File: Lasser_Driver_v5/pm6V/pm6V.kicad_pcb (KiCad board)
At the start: 2 copper layers, 160 x 100 mm, 62 parts, among them J4 Screw_Terminal_01x03, J6 DIN41612_M_3x8+8_Power_Male, Q10 Q_NPN MJL21194, Q3 IRF540NPBF, Q4 IRF9540NPBF, Q5 MMBT2907, Q6 MMBT2222, Q7 Q_PNP_MJL21193, Q8 Q_PNP_MJL21193, Q9 Q_NPN MJL21194, U11 LM4051AIM3-ADJ/NOPB, U12 LM4051AIM3-ADJ/NOPB

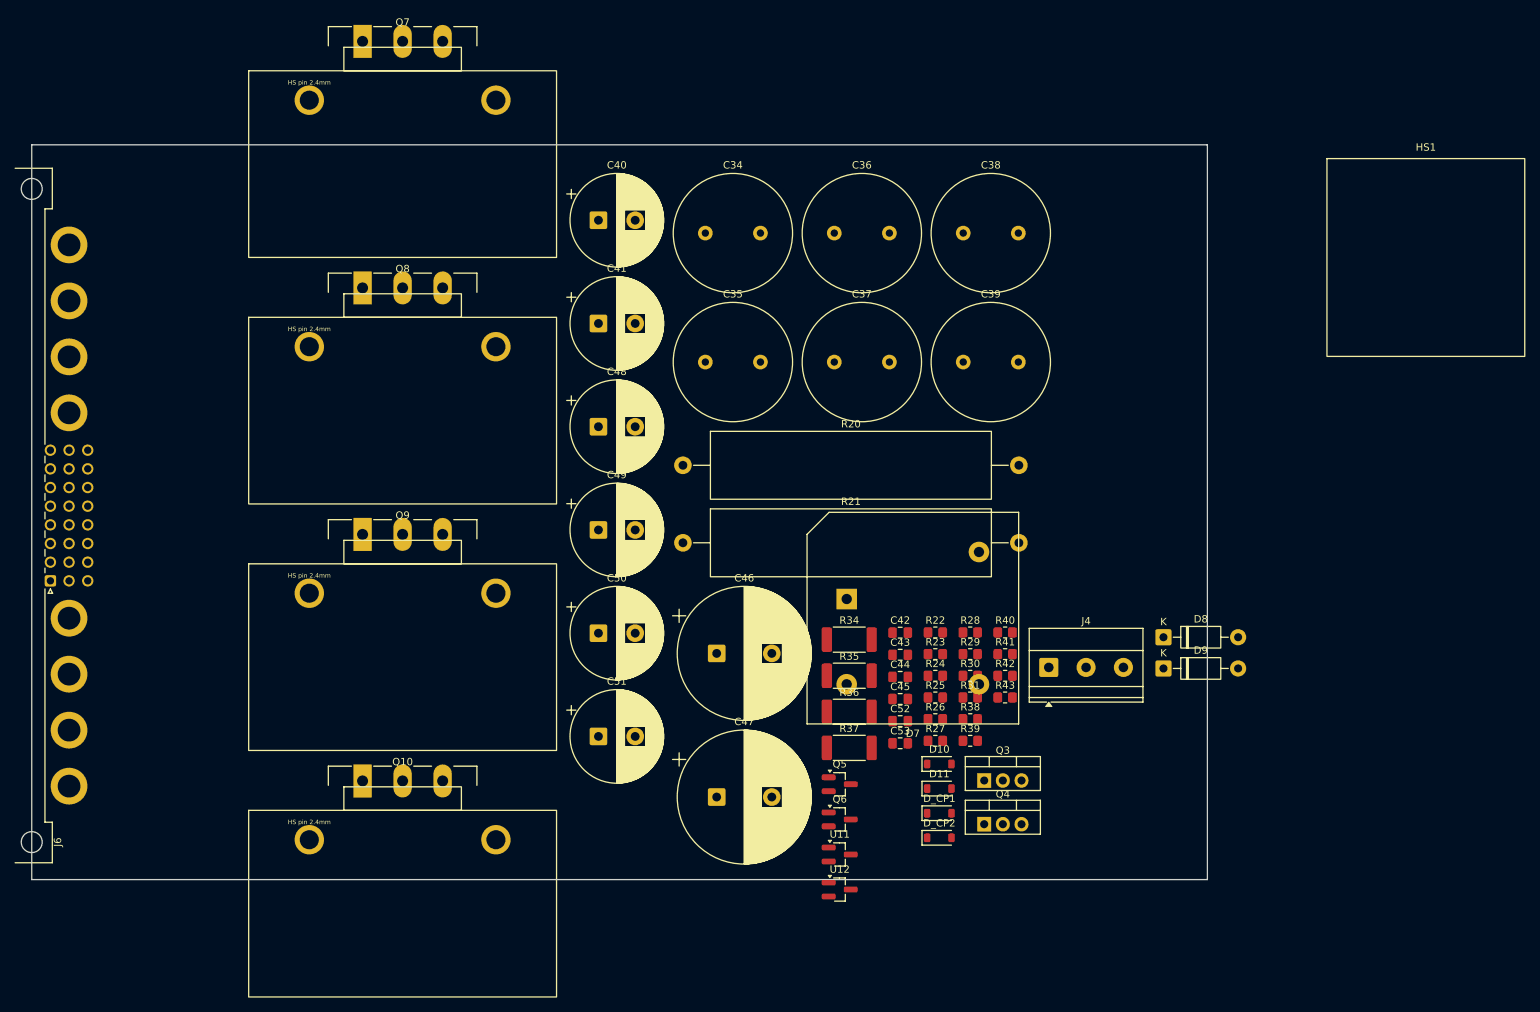
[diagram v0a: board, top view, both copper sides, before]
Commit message: pm6V PCB finished.  Started last power board.
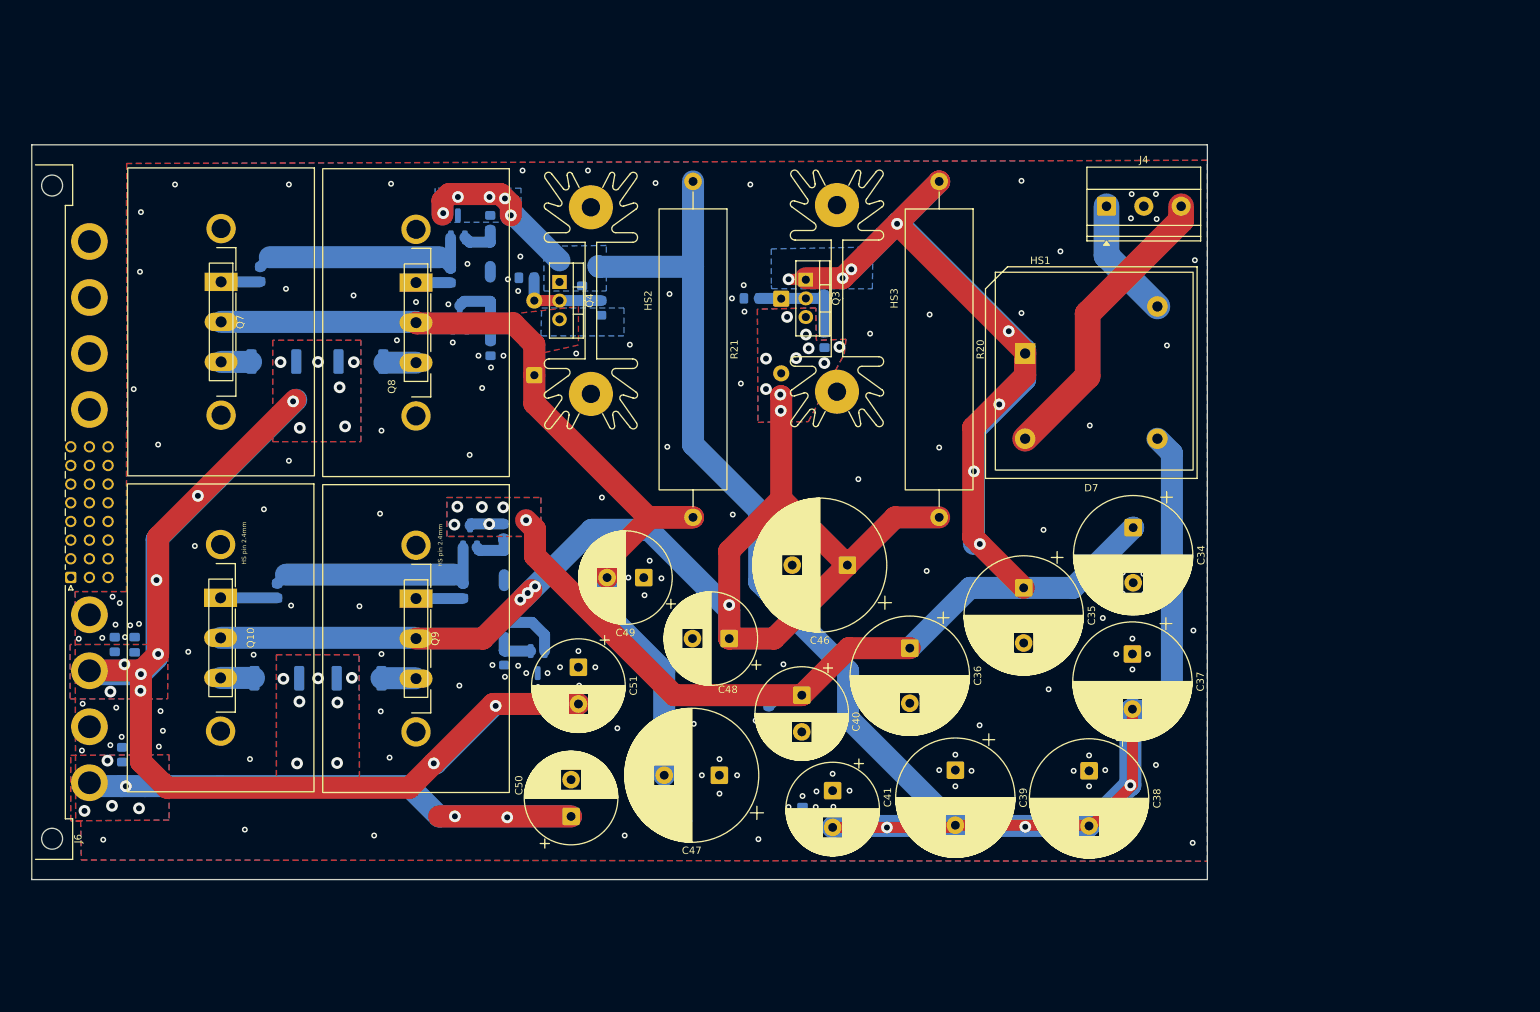
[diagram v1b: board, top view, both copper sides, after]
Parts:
- added HS2: Heatsink Boyd 531102B02500G, Heatsink:Heatsink_AAVID_Extruded_531102B02500G_34.9x12.7mm_H38.1mm, F.Cu at (131.1, 66.2)
- added HS3: Heatsink Boyd 531102B02500G, Heatsink:Heatsink_AAVID_Extruded_531102B02500G_34.9x12.7mm_H38.1mm, F.Cu at (164.6, 65.9)
- C34, C35, C36, C37, C38, C39: footprint Capacitor_THT:C_Radial_D16.0mm_H25.0mm_P7.50mm -> Capacitor_THT:CP_Radial_D16.0mm_P7.50mm
- C42, C43, C44, C45, C52, C53, D10, D11, D8, D9, D_CP1, D_CP2, Q5, Q6, R24, R25, R28, R29, R30, R31, R34, R35, R36, R37, R38, R39, R40, R41, R42, R43, U11, U12: moved to B.Cu
- D7: value GBPC1510-E4/51 -> GBPC1510W-E4/51
- Q10, Q7, Q8, Q9: footprint Heatsinks:TO-264-3_Vertical_HS657-25ABPE -> Heatsinks:TO-264-3_Vertical_HS657-10ABPE
- Q3: value IRF540NPBF -> IRF540ZPBF
- R22, R23: value 1M -> 100k; moved to B.Cu
- R26, R27: value 100k -> 1M; moved to B.Cu
- moved R39 117.2 mm to (66.3, 113.0), turned to -90 degrees
- moved R38 115.5 mm to (67.3, 128.0), turned to 90 degrees
- moved R42 115.2 mm to (86.1, 62.6), turned to -90 degrees
- moved C53 105.1 mm to (69.0, 113.0), turned to -90 degrees
- moved C52 102.9 mm to (70.4, 127.9), turned to 90 degrees
- moved D_CP2 100.2 mm to (117.4, 59.9), turned to -90 degrees
- moved R41 99.4 mm to (88.4, 105.7), turned to -90 degrees
- moved R43 94.8 mm to (112.0, 62.8), turned to -90 degrees
- moved Q4 93.7 mm to (126.8, 63.7), turned to -90 degrees
- moved U12 93.5 mm to (113.2, 68.4), turned to 90 degrees
- moved D8 92.8 mm to (123.4, 76.4), turned to 90 degrees
- moved Q5 92.0 mm to (113.0, 56.1), turned to 90 degrees
- moved D11 91.4 mm to (117.4, 64.7), turned to -90 degrees
- moved R29 87.8 mm to (117.4, 55.6), turned to -90 degrees
- moved R34 87.0 mm to (88.0, 74.5), turned to 180 degrees
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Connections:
- C37 pad 1: /TEC_RAW- -> DGND
- C37 pad 2: DGND -> /TEC_RAW-
- C38 pad 1: /TEC_RAW- -> DGND
- C38 pad 2: DGND -> /TEC_RAW-
- C39 pad 1: /TEC_RAW- -> DGND
- C39 pad 2: DGND -> /TEC_RAW-
- C41 pad 1: /TEC_RAW- -> DGND
- C41 pad 2: DGND -> /TEC_RAW-
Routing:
- net /TEC_RAW-: track 0.00 -> 291.8 mm, vias 0 -> 8
- net /TEC_RAW+: track 0.00 -> 273.1 mm, vias 0 -> 14
- net -6V_TEC: track 0.00 -> 206.2 mm, vias 0 -> 16
- net Net-(D9-A): track 0.00 -> 169.6 mm, vias 0 -> 14
- net Net-(D8-K): track 0.00 -> 126.5 mm
- net +6V_TEC: track 0.00 -> 85.5 mm, vias 0 -> 14
- net +9Vac: track 0.00 -> 40.4 mm
- net Net-(Q5-E): track 0.00 -> 31.2 mm
- net Net-(Q6-E): track 0.00 -> 31.2 mm
- net -9Vac: track 0.00 -> 16.5 mm
- net Net-(D9-K): track 0.00 -> 14.3 mm
- net Net-(D8-A): track 0.00 -> 12.2 mm
- net Net-(D10-K): track 0.00 -> 10.1 mm
- net Net-(Q10-B): track 0.00 -> 7.72 mm
- net Net-(Q9-B): track 0.00 -> 6.42 mm
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- added copper zone on B.Cu, net +6V_TEC
- added copper zone on F.Cu, net +6V_TEC
- added copper zone on B.Cu, net -6V_TEC
- added copper zone on F.Cu, net -6V_TEC
- added copper zone on B.Cu, net /TEC_RAW+
- added copper zone on F.Cu, net /TEC_RAW+
- added copper zone on B.Cu, net /TEC_RAW-
- added copper zone on B.Cu, net DGND
- added copper zone on F.Cu, net DGND
- added copper zone on B.Cu, net Net-(D8-K)
- added copper zone on F.Cu, net Net-(D8-K)
- added copper zone on B.Cu, net Net-(D9-A)
- added copper zone on F.Cu, net Net-(D9-A)

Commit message: Figured out remaining cards.
Created backplane pcb.  Should be ready to go to fab just need BOM.  Layout matches standard for hole spacing.
Updated Teensy code to match pinout and updated schematics.
Changed DGND to TECGND for clarity.
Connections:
- net DGND renamed PGND_TEC

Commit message: working on the digital pcb layout.  Mostly done.
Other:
- board text added: "HEATSINK ISSUE (Q7-Q10): 657-10ABPE DOES NOT FIT THE TO-264 (channel ~16mm < 20mm device). UPDATE to clip-on heatsink OMNI-UNI-PF-38 + OMNI-UC clip (Wakefield-Vette; DK 345-1600-ND / 345-1493-ND). Clip mount: existing 25.4mm pin holes go unused. Trialing before permanent change."
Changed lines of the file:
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@@
+		)
+	)
+	(gr_text "HEATSINK ISSUE (Q7-Q10): 657-10ABPE DOES NOT FIT THE TO-264 (channel ~16mm < 20mm device).\nUPDATE to clip-on heatsink OMNI-UNI-PF-38 + OMNI-UC clip (Wakefield-Vette; DK 345-1600-ND / 345-1493-ND).\nClip mount: existing 25.4mm pin holes go unused. Trialing before permanent change."
+		(at 55.5 154 0)
+		(layer "Cmts.User")
+		(effects
+			(font
+				(size 1 1)
+				(thickness 0.15)
+			)
+			(justify left)
 		)
 	)
